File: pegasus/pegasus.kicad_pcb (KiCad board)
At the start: 2 copper layers, 50 x 120 mm, 15 parts, among them IC1 RFD900, IC2 Adafruit_MPL3115A2, IC3 Adafruit-BNO055-PCB, IC4 L70B-M39, IC5 L7805ACV, J1 Conn_01x02_Female, J2 Conn_01x02_Female, U1 Teensy4.1, U2 CON-SMA-EDGE-S, U3 CON-SMA-EDGE-S

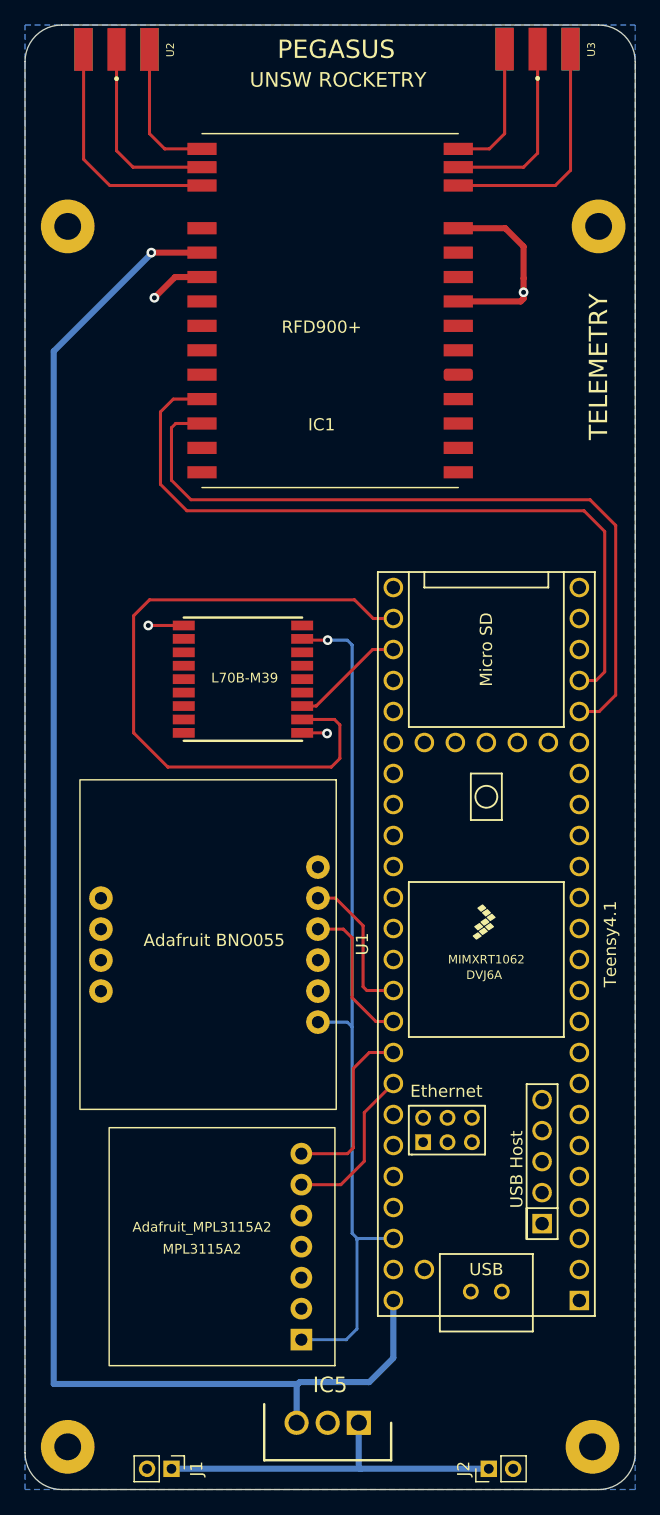
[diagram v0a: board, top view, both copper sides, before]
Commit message: modified some trace lengths
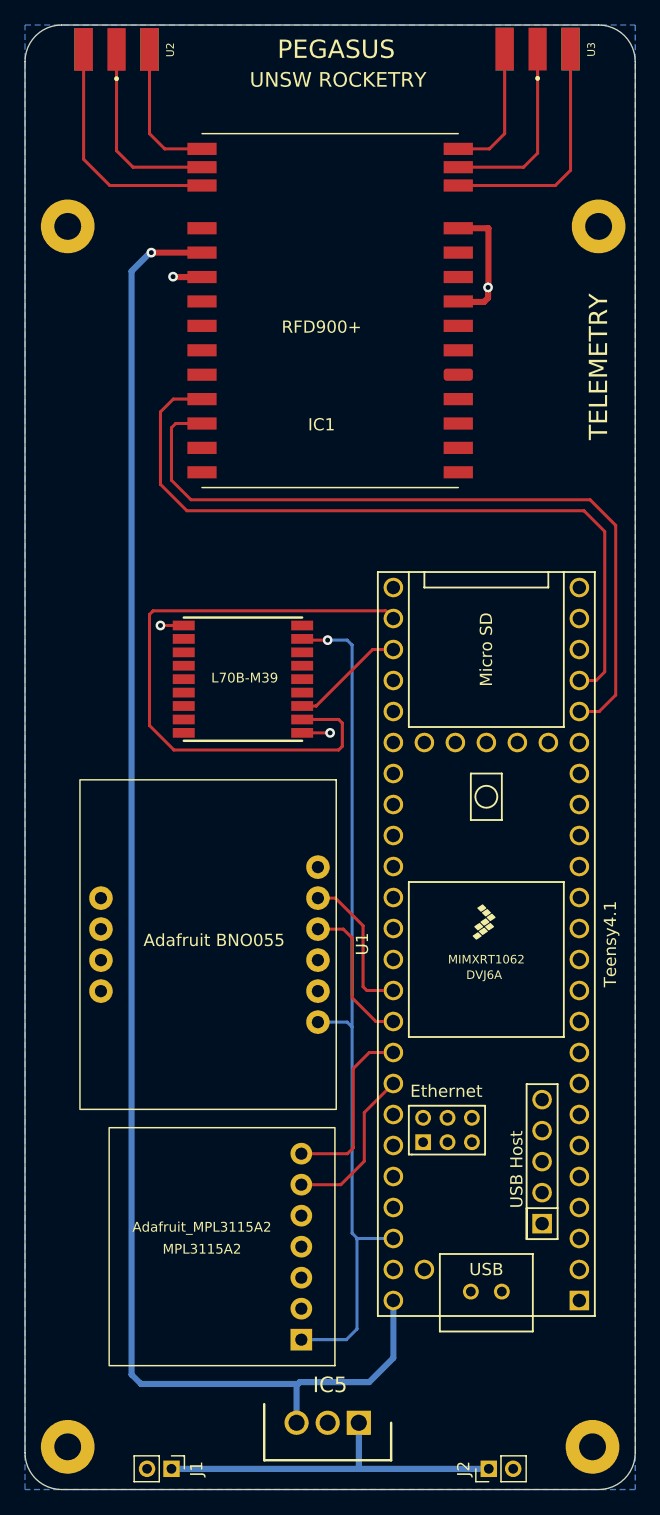
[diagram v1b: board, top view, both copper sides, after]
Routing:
- net +5V: track 137.0 -> 127.5 mm
- net GND: track 25.3 -> 17.4 mm
- net RX8: track 56.4 -> 51.5 mm
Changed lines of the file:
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@@
     (effects (font (size 1.2 1.2) (thickness 0.2)))
   )
-  (segment (start 115.5 56.65) (end 119.35 56.65) (width 0.5) (layer "F.Cu") (net 2))
-  (segment (start 104.7 98) (end 104.75 98.05) (width 0.25) (layer "F.Cu") (net 2))
-  (segment (start 115.5 62.65) (end 120.62 62.65) (width 0.5) (layer "F.Cu") (net 2))
-  (segment (start 120.62 62.65) (end 120.85 62.42) (width 0.5) (layer "F.Cu") (net 2))
-  (segment (start 90.1 89.2) (end 93.007 89.2) (width 0.25) (layer "F.Cu") (net 2))
-  (segment (start 92.3 60.65) (end 90.6 62.35) (width 0.5) (layer "F.Cu") (net 2))
-  (segment (start 120.85 60.75) (end 120.85 61.9) (width 0.5) (layer "F.Cu") (net 2))
-  (segment (start 120.85 62.42) (end 120.85 61.9) (width 0.5) (layer "F.Cu") (net 2))
-  (segment (start 102.707 98) (end 104.7 98) (width 0.25) (layer "F.Cu") (net 2))
-  (segment (start 119.35 56.65) (end 120.85 58.15) (width 0.5) (layer "F.Cu") (net 2))
-  (segment (start 94.5 60.65) (end 92.3 60.65) (width 0.5) (layer "F.Cu") (net 2))
-  (segment (start 120.85 58.15) (end 120.85 60.75) (width 0.5) (layer "F.Cu") (net 2))
-  (via (at 90.6 62.35) (size 0.8) (drill 0.4) (layers "F.Cu" "B.Cu") (net 2))
-  (via (at 104.75 98.05) (size 0.8) (drill 0.4) (layers "F.Cu" "B.Cu") (free) (net 2))
-  (via (at 120.85 61.9) (size 0.8) (drill 0.4) (layers "F.Cu" "B.Cu") (net 2))
-  (via (at 90.1 89.2) (size 0.8) (drill 0.4) (layers "F.Cu" "B.Cu") (free) (net 2))
+  (segment (start 92.36 60.65) (end 94.5 60.65) (width 0.5) (layer "F.Cu") (net 2))
+  (segment (start 92.13 60.62) (end 92.33 60.62) (width 0.5) (layer "F.Cu") (net 2))
+  (segment (start 117.61 62.69) (end 115.54 62.69) (width 0.5) (layer "F.Cu") (net 2))
+  (segment (start 117.94 61.5) (end 117.94 62.36) (width 0.5) (layer "F.Cu") (net 2))
+  (segment (start 117.97 61.47) (end 117.97 56.66) (width 0.5) (layer "F.Cu") (net 2))
+  (segment (start 117.96 56.65) (end 115.5 56.65) (width 0.5) (layer "F.Cu") (net 2))
+  (segment (start 115.54 62.69) (end 115.5 62.65) (width 0.5) (layer "F.Cu") (net 2))
+  (segment (start 117.94 61.5) (end 117.97 61.47) (width 0.5) (layer "F.Cu") (net 2))
+  (segment (start 91.1 89.2) (end 93.007 89.2) (width 0.25) (layer "F.Cu") (net 2))
+  (segment (start 117.97 56.66) (end 117.96 56.65) (width 0.5) (layer "F.Cu") (net 2))
+  (segment (start 117.94 62.36) (end 117.61 62.69) (width 0.5) (layer "F.Cu") (net 2))
+  (segment (start 92.33 60.62) (end 92.36 60.65) (width 0.5) (layer "F.Cu") (net 2))
+  (segment (start 105 98) (end 102.707 98) (width 0.25) (layer "F.Cu") (net 2))
+  (via (at 92.13 60.62) (size 0.8) (drill 0.4) (layers "F.Cu" "B.Cu") (net 2))
+  (via (at 105 98) (size 0.8) (drill 0.4) (layers "F.Cu" "B.Cu") (free) (net 2))
+  (via (at 117.94 61.5) (size 0.8) (drill 0.4) (layers "F.Cu" "B.Cu") (net 2))
+  (via (at 91.1 89.2) (size 0.8) (drill 0.4) (layers "F.Cu" "B.Cu") (free) (net 2))
   (segment (start 124.7 51.9) (end 124.7 41.9725) (width 0.25) (layer "F.Cu") (net 10))
   (segment (start 123.45 53.15) (end 124.7 51.9) (width 0.25) (layer "F.Cu") (net 10))
@@
   (segment (start 86.95 53.15) (end 84.8 51) (width 0.25) (layer "F.Cu") (net 15))
   (segment (start 84.8 51) (end 84.8 42) (width 0.25) (layer "F.Cu") (net 15))
-  (segment (start 91.7 100.8) (end 88.9 98) (width 0.25) (layer "F.Cu") (net 96))
-  (segment (start 105.8 97.35) (end 105.8 100.1) (width 0.25) (layer "F.Cu") (net 96))
-  (segment (start 88.9 88.4) (end 90.2 87.1) (width 0.25) (layer "F.Cu") (net 96))
-  (segment (start 107 87.1) (end 108.53 88.63) (width 0.25) (layer "F.Cu") (net 96))
-  (segment (start 108.53 88.63) (end 110.18 88.63) (width 0.25) (layer "F.Cu") (net 96))
-  (segment (start 88.9 98) (end 88.9 88.4) (width 0.25) (layer "F.Cu") (net 96))
-  (segment (start 105.35 96.9) (end 105.8 97.35) (width 0.25) (layer "F.Cu") (net 96))
-  (segment (start 105.1 100.8) (end 91.7 100.8) (width 0.25) (layer "F.Cu") (net 96))
-  (segment (start 90.2 87.1) (end 107 87.1) (width 0.25) (layer "F.Cu") (net 96))
-  (segment (start 102.707 96.9) (end 105.35 96.9) (width 0.25) (layer "F.Cu") (net 96))
-  (segment (start 105.8 100.1) (end 105.1 100.8) (width 0.25) (layer "F.Cu") (net 96))
+  (segment (start 90.5 88) (end 109.55 88) (width 0.25) (layer "F.Cu") (net 96))
+  (segment (start 106 99.1) (end 105.7 99.4) (width 0.25) (layer "F.Cu") (net 96))
+  (segment (start 90.2 97.4) (end 90.2 88.3) (width 0.25) (layer "F.Cu") (net 96))
+  (segment (start 92.2 99.4) (end 90.2 97.4) (width 0.25) (layer "F.Cu") (net 96))
+  (segment (start 109.55 88) (end 110.18 88.63) (width 0.25) (layer "F.Cu") (net 96))
+  (segment (start 105.7 96.9) (end 106 97.2) (width 0.25) (layer "F.Cu") (net 96))
+  (segment (start 106 97.2) (end 106 99.1) (width 0.25) (layer "F.Cu") (net 96))
+  (segment (start 90.2 88.3) (end 90.5 88) (width 0.25) (layer "F.Cu") (net 96))
+  (segment (start 105.7 99.4) (end 92.2 99.4) (width 0.25) (layer "F.Cu") (net 96))
+  (segment (start 102.707 96.9) (end 105.7 96.9) (width 0.25) (layer "F.Cu") (net 96))
   (segment (start 103.857 95.8) (end 108.487 91.17) (width 0.25) (layer "F.Cu") (net 97))
   (segment (start 102.707 95.8) (end 103.857 95.8) (width 0.25) (layer "F.Cu") (net 97))
@@
   (segment (start 90.35 58.65) (end 94.5 58.65) (width 0.5) (layer "F.Cu") (net 105))
   (via (at 90.35 58.65) (size 0.8) (drill 0.4) (layers "F.Cu" "B.Cu") (net 105))
+  (segment (start 89.5 151.35) (end 88.73 150.58) (width 0.5) (layer "B.Cu") (net 105))
   (segment (start 110.18 149.22) (end 110.18 144.51) (width 0.5) (layer "B.Cu") (net 105))
   (segment (start 102.25 151.45) (end 102.5 151.2) (width 0.25) (layer "B.Cu") (net 105))
-  (segment (start 102.35 151.35) (end 82.35 151.35) (width 0.5) (layer "B.Cu") (net 105))
+  (segment (start 88.73 60.17) (end 90.25 58.65) (width 0.5) (layer "B.Cu") (net 105))
   (segment (start 102.25 154.53) (end 102.25 151.45) (width 0.5) (layer "B.Cu") (net 105))
+  (segment (start 102.35 151.35) (end 89.5 151.35) (width 0.5) (layer "B.Cu") (net 105))
   (segment (start 102.5 151.2) (end 102.35 151.35) (width 0.5) (layer "B.Cu") (net 105))
-  (segment (start 90.25 58.83) (end 90.25 58.65) (width 0.5) (layer "B.Cu") (net 105))
   (segment (start 108.2 151.2) (end 110.18 149.22) (width 0.5) (layer "B.Cu") (net 105))
-  (segment (start 82.35 151.35) (end 82.35 66.73) (width 0.5) (layer "B.Cu") (net 105))
-  (segment (start 82.35 66.73) (end 90.25 58.83) (width 0.5) (layer "B.Cu") (net 105))
   (segment (start 102.5 151.2) (end 108.2 151.2) (width 0.5) (layer "B.Cu") (net 105))
+  (segment (start 88.73 150.58) (end 88.73 60.17) (width 0.5) (layer "B.Cu") (net 105))
   (segment (start 107.5 158.3) (end 107.35 158.15) (width 0.25) (layer "B.Cu") (net 106))
   (segment (start 118 158.3) (end 107.5 158.3) (width 0.5) (layer "B.Cu") (net 106))
